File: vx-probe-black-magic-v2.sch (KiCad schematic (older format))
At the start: 41 parts, among them P1 USB MINI B, P10 CONN_01X01, P11 CONN_01X11, P2 +5v power input, P3 +5v external input, P4 CONN_02X05, P5 CONN_01X04, P6 swdio/jtag, P7 CONN_01X01, P8 CONN_01X01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

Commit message: reorganized the unused pins connector
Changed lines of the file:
@@
 Text Label 3750 3650 0    60   ~ 0
 x2
-Text Label 1400 3600 0    60   ~ 0
+Text Label 1400 4100 0    60   ~ 0
 x2
 Text Label 1400 3500 0    60   ~ 0
@@
 Text Label 3750 3750 0    60   ~ 0
 x3
-Text Label 1400 4100 0    60   ~ 0
+Text Label 1400 3900 0    60   ~ 0
 x4
 Text Label 3750 4350 0    60   ~ 0
@@
 Text Label 5400 5900 1    60   ~ 0
 x5
-Text Label 1400 4000 0    60   ~ 0
+Text Label 1400 3800 0    60   ~ 0
 x5
-Text Label 1400 3900 0    60   ~ 0
+Text Label 1400 3700 0    60   ~ 0
 x6
 Text Label 5500 5900 1    60   ~ 0
@@
 Text Label 5600 6150 1    60   ~ 0
 x7
-Text Label 1400 3700 0    60   ~ 0
+Text Label 1400 3600 0    60   ~ 0
 x7
 $Comp

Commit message: placed and routed the reset button and a serial port
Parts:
- added P12: CONN_01X03, Pin_Headers:Pin_Header_Straight_1x03, symbol CONN_01X03
- added SW1: SW_PUSH, Buttons_Switches_ThroughHole:SW_PUSH_6mm, symbol SW_PUSH
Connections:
- net labels added: U1_RX, U1_TX
- wire segments 152 -> 161
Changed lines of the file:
@@
 Text Label 1400 3400 0    60   ~ 0
 x8
+$Comp
+L SW_PUSH SW1
+U 1 1 57DC876B
+P 3900 1550
+F 0 "SW1" H 4050 1660 50  0000 C CNN
+F 1 "SW_PUSH" H 3900 1470 50  0000 C CNN
+F 2 "Buttons_Switches_ThroughHole:SW_PUSH_6mm" H 3900 1550 50  0001 C CNN
+F 3 "" H 3900 1550 50  0000 C CNN
+	1    3900 1550
+	1    0    0    -1
+$EndComp
+Wire Wire Line
+	4200 1550 4300 1550
+Wire Wire Line
+	3600 1550 3500 1550
+Wire Wire Line
+	4300 1550 4300 1600
+$Comp
+L GND #PWR021
+U 1 1 57DC92C3
+P 4300 1600
+F 0 "#PWR021" H 4300 1350 50  0001 C CNN
+F 1 "GND" H 4300 1450 50  0000 C CNN
+F 2 "" H 4300 1600 50  0000 C CNN
+F 3 "" H 4300 1600 50  0000 C CNN
+	1    4300 1600
+	1    0    0    -1
+$EndComp
+Text Label 3500 1550 2    60   ~ 0
+PROG_NRST
+Wire Wire Line
+	7300 3950 7700 3950
+Wire Wire Line
+	7300 4050 7700 4050
+Text Label 7350 3950 0    60   ~ 0
+U1_RX
+Text Label 7350 4050 0    60   ~ 0
+U1_TX
+$Comp
+L CONN_01X03 P12
+U 1 1 57DCA345
+P 3100 2550
+F 0 "P12" H 3100 2750 50  0000 C CNN
+F 1 "CONN_01X03" V 3200 2550 50  0000 C CNN
+F 2 "Pin_Headers:Pin_Header_Straight_1x03" H 3100 2550 50  0001 C CNN
+F 3 "" H 3100 2550 50  0000 C CNN
+	1    3100 2550
+	-1   0    0    1
+$EndComp
+Wire Wire Line
+	3300 2450 3400 2450
+Wire Wire Line
+	3300 2550 3400 2550
+Wire Wire Line
+	3300 2650 3400 2650
+Wire Wire Line
+	3400 2650 3400 2700
+$Comp
+L GND #PWR022
+U 1 1 57DCA85F
+P 3400 2700
+F 0 "#PWR022" H 3400 2450 50  0001 C CNN
+F 1 "GND" H 3400 2550 50  0000 C CNN
+F 2 "" H 3400 2700 50  0000 C CNN
+F 3 "" H 3400 2700 50  0000 C CNN
+	1    3400 2700
+	1    0    0    -1
+$EndComp
+Text Label 3400 2450 0    60   ~ 0
+U1_RX
+Text Label 3400 2550 0    60   ~ 0
+U1_TX
 $EndSCHEMATC

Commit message: added a pull-up resistor on the target power enable switch (pmosfet)
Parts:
- added R12: 10k, Resistors_SMD:R_0805, symbol R
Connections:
- wire segments 161 -> 162
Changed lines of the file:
@@
 Wire Wire Line
 	12650 5800 12650 5950
-Wire Wire Line
-	11950 5600 12350 5600
-Text Label 11950 5600 0    60   ~ 0
+Text Label 12150 5600 2    60   ~ 0
 TPWR_CTRL
 Wire Wire Line
@@
 Text Label 3400 2550 0    60   ~ 0
 U1_TX
+Wire Wire Line
+	12350 5600 12150 5600
+Wire Wire Line
+	12300 5600 12300 5500
+Connection ~ 12300 5600
+$Comp
+L R R12
+U 1 1 57DCC3D9
+P 12300 5350
+F 0 "R12" H 12380 5350 50  0000 C CNN
+F 1 "10k" V 12300 5350 50  0000 C CNN
+F 2 "Resistors_SMD:R_0805" V 12230 5350 50  0001 C CNN
+F 3 "" H 12300 5350 50  0000 C CNN
+	1    12300 5350
+	1    0    0    -1
+$EndComp
+$Comp
+L +3V3 #PWR023
+U 1 1 57DCC44A
+P 12300 5200
+F 0 "#PWR023" H 12300 5050 50  0001 C CNN
+F 1 "+3V3" H 12300 5340 50  0000 C CNN
+F 2 "" H 12300 5200 50  0000 C CNN
+F 3 "" H 12300 5200 50  0000 C CNN
+	1    12300 5200
+	1    0    0    -1
+$EndComp
 $EndSCHEMATC

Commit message: changed the jtag and uext connectors to idc headers
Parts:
- P4, P6: footprint Pin_Headers:Pin_Header_Straight_2x05 -> Connect:IDC_Header_Straight_10pins
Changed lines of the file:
@@
 F 0 "P4" H 9800 3050 50  0000 C CNN
 F 1 "CONN_02X05" H 9800 2450 50  0000 C CNN
-F 2 "Pin_Headers:Pin_Header_Straight_2x05" H 9800 1550 50  0001 C CNN
+F 2 "Connect:IDC_Header_Straight_10pins" H 9800 1550 50  0001 C CNN
 F 3 "" H 9800 1550 50  0000 C CNN
 	1    9800 2750
@@
 F 0 "P6" H 5400 7200 50  0000 C CNN
 F 1 "swdio/jtag" H 5400 7350 50  0000 C CNN
-F 2 "Pin_Headers:Pin_Header_Straight_2x05" H 5400 5700 50  0001 C CNN
+F 2 "Connect:IDC_Header_Straight_10pins" H 5400 5700 50  0001 C CNN
 F 3 "" H 5400 5700 50  0000 C CNN
 	1    5400 6900

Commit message: added a button
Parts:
- added R13: 10k, Resistors_SMD:R_0805, symbol R
- added SW2: SW_PUSH, Buttons_Switches_ThroughHole:SW_PUSH_6mm, symbol SW_PUSH
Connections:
- net labels added: BTN1
- net labels removed: x8
- wire segments 162 -> 166
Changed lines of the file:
@@
 TPWR
 Text Label 6000 6150 1    60   ~ 0
-x8
-Text Label 1400 3400 0    60   ~ 0
-x8
+BTN1
 $Comp
 L SW_PUSH SW1
@@
 	1    0    0    -1
 $EndComp
+$Comp
+L SW_PUSH SW2
+U 1 1 57DD33A0
+P 3900 1050
+F 0 "SW2" H 4050 1160 50  0000 C CNN
+F 1 "SW_PUSH" H 3900 970 50  0000 C CNN
+F 2 "Buttons_Switches_ThroughHole:SW_PUSH_6mm" H 3900 1050 50  0001 C CNN
+F 3 "" H 3900 1050 50  0000 C CNN
+	1    3900 1050
+	1    0    0    -1
+$EndComp
+Wire Wire Line
+	3600 1050 3500 1050
+Text Label 3500 1050 2    60   ~ 0
+BTN1
+Wire Wire Line
+	4200 1050 4300 1050
+Wire Wire Line
+	4300 1050 4300 1000
+$Comp
+L R R13
+U 1 1 57DD46EB
+P 4300 850
+F 0 "R13" H 4400 850 50  0000 C CNN
+F 1 "10k" V 4300 850 50  0000 C CNN
+F 2 "Resistors_SMD:R_0805" V 4230 850 50  0001 C CNN
+F 3 "" H 4300 850 50  0000 C CNN
+	1    4300 850
+	1    0    0    -1
+$EndComp
+Wire Wire Line
+	4300 700  4300 650
+$Comp
+L +3V3 #PWR024
+U 1 1 57DD4877
+P 4300 650
+F 0 "#PWR024" H 4300 500 50  0001 C CNN
+F 1 "+3V3" H 4300 790 50  0000 C CNN
+F 2 "" H 4300 650 50  0000 C CNN
+F 3 "" H 4300 650 50  0000 C CNN
+	1    4300 650
+	1    0    0    -1
+$EndComp

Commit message: added another button - this adds 4 vias!!!
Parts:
- added R14: 10k, Resistors_SMD:R_0805, symbol R
- added SW3: SW_PUSH, Buttons_Switches_ThroughHole:SW_PUSH_6mm, symbol SW_PUSH
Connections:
- net labels added: BTN2
- net labels removed: x1
- wire segments 166 -> 170
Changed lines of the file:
@@
 Wire Wire Line
 	5200 5650 5200 5900
-Text Label 1400 4200 0    60   ~ 0
-x1
+Text Label 5550 1050 2    60   ~ 0
+BTN2
 Text Label 3750 3550 0    60   ~ 0
-x1
+BTN2
 $Comp
 L CONN_01X11 P11
@@
 	1    0    0    -1
 $EndComp
+$Comp
+L SW_PUSH SW3
+U 1 1 57DF936B
+P 5950 1050
+F 0 "SW3" H 6100 1160 50  0000 C CNN
+F 1 "SW_PUSH" H 5950 970 50  0000 C CNN
+F 2 "Buttons_Switches_ThroughHole:SW_PUSH_6mm" H 5950 1050 50  0001 C CNN
+F 3 "" H 5950 1050 50  0000 C CNN
+	1    5950 1050
+	1    0    0    -1
+$EndComp
+Wire Wire Line
+	5650 1050 5550 1050
+Wire Wire Line
+	6250 1050 6350 1050
+Wire Wire Line
+	6350 1050 6350 1000
+$Comp
+L R R14
+U 1 1 57DF9375
+P 6350 850
+F 0 "R14" H 6450 850 50  0000 C CNN
+F 1 "10k" V 6350 850 50  0000 C CNN
+F 2 "Resistors_SMD:R_0805" V 6280 850 50  0001 C CNN
+F 3 "" H 6350 850 50  0000 C CNN
+	1    6350 850
+	1    0    0    -1
+$EndComp
+Wire Wire Line
+	6350 700  6350 650
+$Comp
+L +3V3 #PWR025
+U 1 1 57DF937C
+P 6350 650
+F 0 "#PWR025" H 6350 500 50  0001 C CNN
+F 1 "+3V3" H 6350 790 50  0000 C CNN
+F 2 "" H 6350 650 50  0000 C CNN
+F 3 "" H 6350 650 50  0000 C CNN
+	1    6350 650
+	1    0    0    -1
+$EndComp

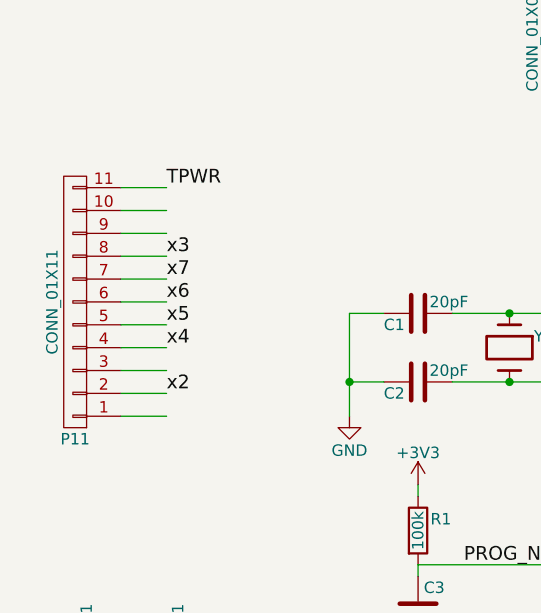
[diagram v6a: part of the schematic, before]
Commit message: rerouted the extension connector
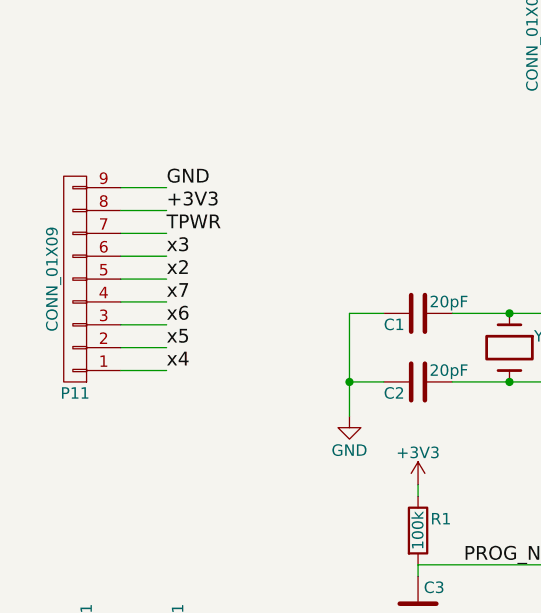
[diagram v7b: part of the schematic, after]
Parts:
- removed P11: CONN_01X11, Pin_Headers:Pin_Header_Straight_1x11, symbol CONN_01X11
- added P11: CONN_01X09, Pin_Headers:Pin_Header_Straight_1x09, symbol CONN_01X09
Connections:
- wire segments 170 -> 168
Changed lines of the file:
@@
 Text Label 3750 3550 0    60   ~ 0
 BTN2
-$Comp
-L CONN_01X11 P11
-U 1 1 57DB0B9D
-P 1000 3700
-F 0 "P11" H 1000 4300 50  0000 C CNN
-F 1 "CONN_01X11" V 1100 3700 50  0000 C CNN
-F 2 "Pin_Headers:Pin_Header_Straight_1x11" H 1000 3700 50  0001 C CNN
-F 3 "" H 1000 3700 50  0000 C CNN
-	1    1000 3700
-	-1   0    0    1
-$EndComp
-Wire Wire Line
-	1200 4200 1400 4200
-Wire Wire Line
-	1200 4100 1400 4100
 Wire Wire Line
 	1200 4000 1400 4000
@@
 Wire Wire Line
 	1200 3400 1400 3400
-Wire Wire Line
-	1200 3300 1400 3300
-Wire Wire Line
-	1200 3200 1400 3200
 Text Label 3750 3650 0    60   ~ 0
 x2
-Text Label 1400 4100 0    60   ~ 0
+Text Label 1400 3600 0    60   ~ 0
 x2
 Text Label 1400 3500 0    60   ~ 0
@@
 Text Label 3750 3750 0    60   ~ 0
 x3
-Text Label 1400 3900 0    60   ~ 0
+Text Label 1400 4000 0    60   ~ 0
 x4
 Text Label 3750 4350 0    60   ~ 0
@@
 Text Label 5400 5900 1    60   ~ 0
 x5
+Text Label 1400 3900 0    60   ~ 0
+x5
 Text Label 1400 3800 0    60   ~ 0
-x5
-Text Label 1400 3700 0    60   ~ 0
 x6
 Text Label 5500 5900 1    60   ~ 0
@@
 Text Label 5600 6150 1    60   ~ 0
 x7
-Text Label 1400 3600 0    60   ~ 0
+Text Label 1400 3700 0    60   ~ 0
 x7
 $Comp
@@
 Text Label 5900 6150 1    60   ~ 0
 VUSB
-Text Label 1400 3200 0    60   ~ 0
+Text Label 1400 3400 0    60   ~ 0
 TPWR
 Text Label 6000 6150 1    60   ~ 0
@@
 	1    0    0    -1
 $EndComp
+Wire Wire Line
+	1200 3300 1400 3300
+Text Label 1400 3300 0    60   ~ 0
++3V3
+Wire Wire Line
+	1200 3200 1400 3200
+Text Label 1400 3200 0    60   ~ 0
+GND
+$Comp
+L CONN_01X09 P11
+U 1 1 57DFBED3
+P 1000 3600
+F 0 "P11" H 1000 4100 50  0000 C CNN
+F 1 "CONN_01X09" V 1100 3600 50  0000 C CNN
+F 2 "Pin_Headers:Pin_Header_Straight_1x09" H 1000 3600 50  0001 C CNN
+F 3 "" H 1000 3600 50  0000 C CNN
+	1    1000 3600
+	-1   0    0    1
+$EndComp
 $EndSCHEMATC

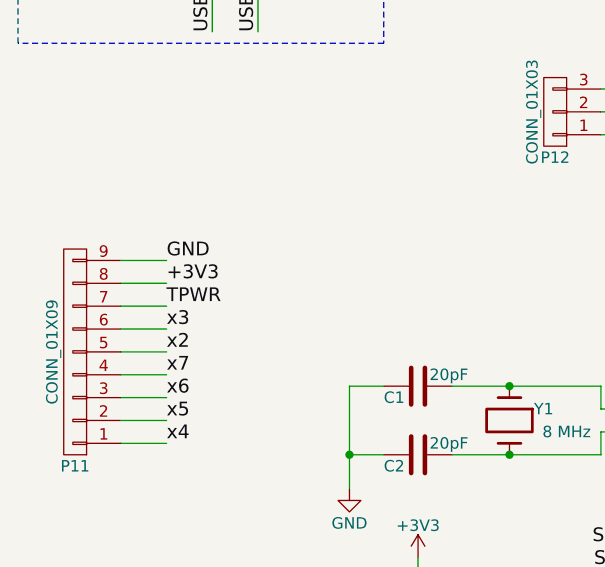
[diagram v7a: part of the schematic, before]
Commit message: optimized extension connector routing
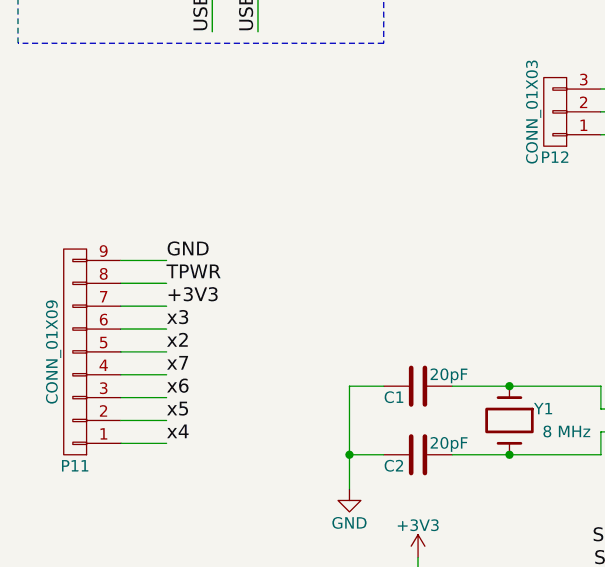
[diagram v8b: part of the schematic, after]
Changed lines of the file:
@@
 Text Label 5900 6150 1    60   ~ 0
 VUSB
-Text Label 1400 3400 0    60   ~ 0
+Text Label 1400 3300 0    60   ~ 0
 TPWR
 Text Label 6000 6150 1    60   ~ 0
@@
 Wire Wire Line
 	1200 3300 1400 3300
-Text Label 1400 3300 0    60   ~ 0
+Text Label 1400 3400 0    60   ~ 0
 +3V3
 Wire Wire Line
